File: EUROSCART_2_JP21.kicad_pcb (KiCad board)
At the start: 2 copper layers, 52.8 x 42.2 mm, 2 parts

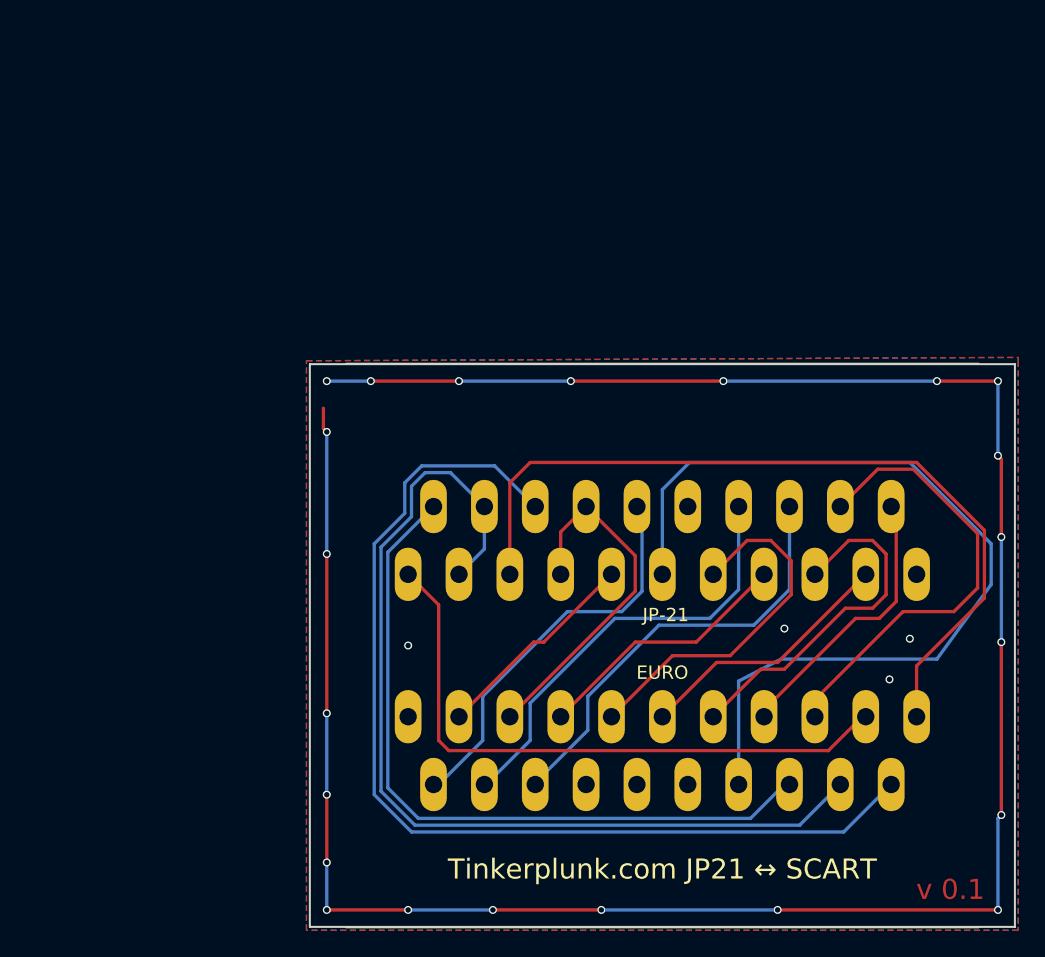
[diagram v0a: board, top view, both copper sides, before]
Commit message: revised to use one female and one male
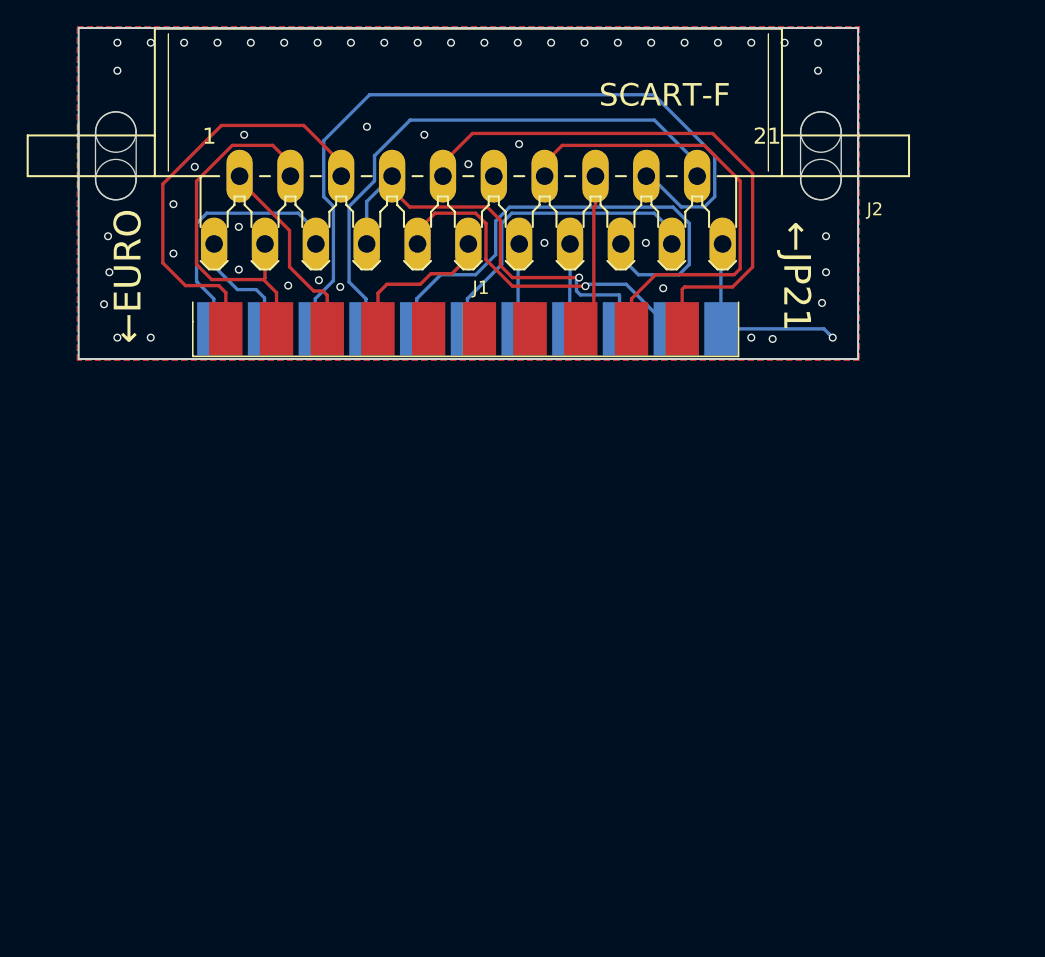
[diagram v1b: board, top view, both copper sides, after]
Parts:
- removed EURO, JP-21: SCART-F, SCART-RIGHT-ANGLE:SCART Right Angle
- added J1: SCART-F, Tinkerplunk:MALE_SCART, F.Cu at (113.2, 93.8)
- added J2: SCART-F, Tinkerplunk:SCART-F-RA, F.Cu at (133.8, 80.4)
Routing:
- net GND: track 178.1 -> 15.1 mm, vias 26 -> 51
- net 5V: track 67.3 -> 11.6 mm
- net RT_IN: track 77.2 -> 31.6 mm
- net A_GND: track 73.3 -> 29.2 mm
- net RT_OUT: track 61.2 -> 19.2 mm
- net L_IN: track 54.6 -> 14.6 mm
- net L_OUT: track 46.8 -> 8.74 mm
- net B_GND: track 34.4 -> 57.8 mm
- net BLU: track 21.1 -> 42.6 mm
- net BLANK: track 32.9 -> 11.9 mm
- net R_GND: track 27.3 -> 6.40 mm
- net RED: track 19.7 -> 6.40 mm
- net S_IN: track 30.1 -> 42.3 mm
- net G_GND: track 26.6 -> 37.6 mm
- net S_OUT: track 15.8 -> 26.7 mm, vias 0 -> 1
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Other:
- board size 52.8 x 42.2 mm -> 58.4 x 24.8 mm
- board text added: "EUROSCART⇄JP21 BIDIRECTIONAL"
- board text added: "←EURO"
- board text added: "←JP21"
- board text removed: "Tinkerplunk.com JP21 ↔ SCART"
- board text removed: "v 0.1"

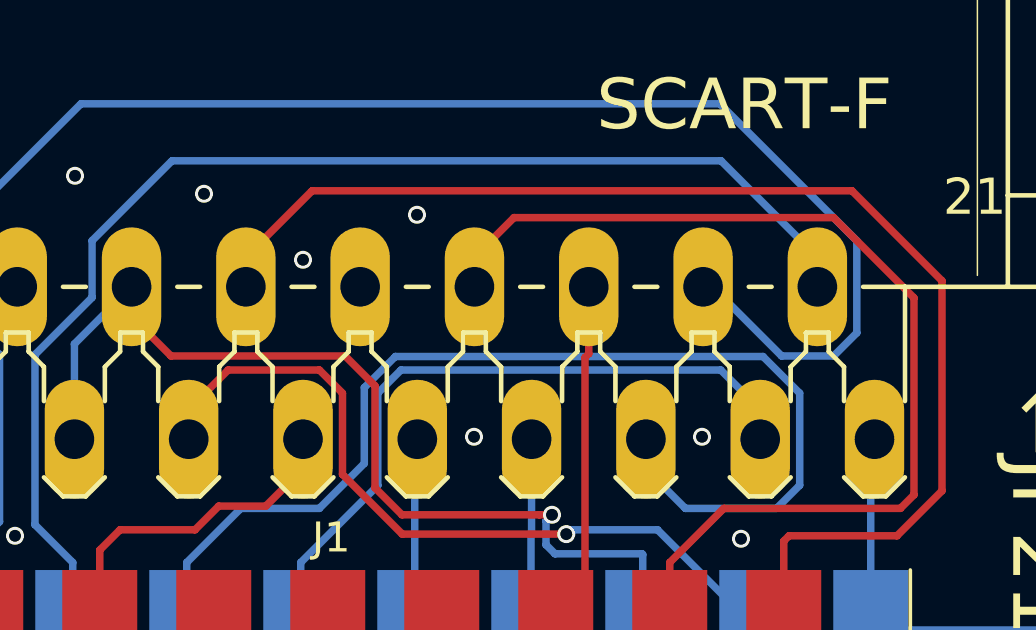
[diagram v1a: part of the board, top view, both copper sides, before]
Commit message: Fixed swapped sync pins on JP21
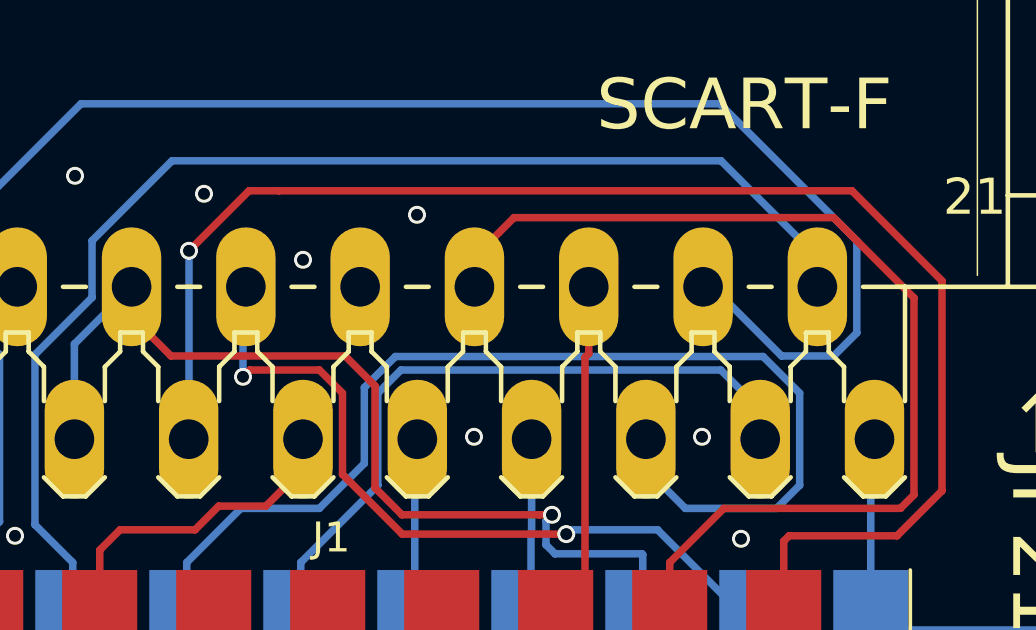
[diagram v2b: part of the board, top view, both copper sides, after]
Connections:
- J2 pad 10: S_IN -> S_OUT
- J2 pad 9: S_OUT -> S_IN
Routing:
- net S_IN: track 42.3 -> 49.4 mm, vias 0 -> 1
- net S_OUT: track 26.7 -> 26.4 mm, vias 1 -> 2
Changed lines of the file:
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@@
     (thickness 1.6)
     (drawings 9)
-    (tracks 208)
+    (tracks 213)
     (zones 0)
     (modules 2)
@@
     (mod_text_size 1 1)
     (mod_text_width 0.15)
-    (pad_size 1.524 1.524)
-    (pad_drill 0.762)
+    (pad_size 3.9624 1.9812)
+    (pad_drill 1.3208)
     (pad_to_mask_clearance 0.2)
     (aux_axis_origin 0 0)
@@
       (net 8 S_GND) (solder_mask_margin 0.1016))
     (pad 9 thru_hole oval (at 3.81 -5.08 270) (size 3.9624 1.9812) (drill 1.3208) (layers *.Cu *.Mask)
+      (net 11 S_IN) (solder_mask_margin 0.1016))
+    (pad 10 thru_hole oval (at 1.905 0 270) (size 3.9624 1.9812) (drill 1.3208) (layers *.Cu *.Mask)
       (net 10 S_OUT) (solder_mask_margin 0.1016))
-    (pad 10 thru_hole oval (at 1.905 0 270) (size 3.9624 1.9812) (drill 1.3208) (layers *.Cu *.Mask)
-      (net 11 S_IN) (solder_mask_margin 0.1016))
     (pad 11 thru_hole oval (at 0 -5.08 270) (size 3.9624 1.9812) (drill 1.3208) (layers *.Cu *.Mask)
       (net 20 5V) (solder_mask_margin 0.1016))
@@
   (gr_line (start 104.6 94.1) (end 163 94.1) (layer Edge.Cuts) (width 0.15))
   (gr_line (start 104.6 69.3) (end 104.6 94.1) (layer Edge.Cuts) (width 0.15))
-  (via (at 160 70.4) (size 0.6) (drill 0.4) (layers F.Cu B.Cu) (net 12))
-  (via (at 157.5 70.4) (size 0.6) (drill 0.4) (layers F.Cu B.Cu) (net 12))
-  (via (at 155 70.4) (size 0.6) (drill 0.4) (layers F.Cu B.Cu) (net 12))
-  (via (at 152.5 70.4) (size 0.6) (drill 0.4) (layers F.Cu B.Cu) (net 12))
-  (via (at 150 70.4) (size 0.6) (drill 0.4) (layers F.Cu B.Cu) (net 12))
-  (via (at 147.5 70.4) (size 0.6) (drill 0.4) (layers F.Cu B.Cu) (net 12))
-  (via (at 145 70.4) (size 0.6) (drill 0.4) (layers F.Cu B.Cu) (net 12))
-  (via (at 142.5 70.4) (size 0.6) (drill 0.4) (layers F.Cu B.Cu) (net 12))
-  (via (at 140 70.4) (size 0.6) (drill 0.4) (layers F.Cu B.Cu) (net 12))
-  (via (at 137.5 70.4) (size 0.6) (drill 0.4) (layers F.Cu B.Cu) (net 12))
-  (via (at 135 70.4) (size 0.6) (drill 0.4) (layers F.Cu B.Cu) (net 12))
-  (via (at 132.5 70.4) (size 0.6) (drill 0.4) (layers F.Cu B.Cu) (net 12))
-  (via (at 130 70.4) (size 0.6) (drill 0.4) (layers F.Cu B.Cu) (net 12))
-  (via (at 127.5 70.4) (size 0.6) (drill 0.4) (layers F.Cu B.Cu) (net 12))
-  (via (at 125 70.4) (size 0.6) (drill 0.4) (layers F.Cu B.Cu) (net 12))
-  (via (at 122.5 70.4) (size 0.6) (drill 0.4) (layers F.Cu B.Cu) (net 12))
-  (via (at 120 70.4) (size 0.6) (drill 0.4) (layers F.Cu B.Cu) (net 12))
-  (via (at 117.5 70.4) (size 0.6) (drill 0.4) (layers F.Cu B.Cu) (net 12))
-  (via (at 115 70.4) (size 0.6) (drill 0.4) (layers F.Cu B.Cu) (net 12))
-  (via (at 112.5 70.4) (size 0.6) (drill 0.4) (layers F.Cu B.Cu) (net 12))
-  (via (at 110 70.4) (size 0.6) (drill 0.4) (layers F.Cu B.Cu) (net 12))
-  (via (at 107.5 70.4) (size 0.6) (drill 0.4) (layers F.Cu B.Cu) (net 12))
   (segment (start 149.04 84.4894) (end 149.04 85.48) (width 0.25) (layer B.Cu) (net 4))
   (segment (start 147.72439 83.17379) (end 149.04 84.4894) (width 0.25) (layer B.Cu) (net 4))
@@
   (segment (start 142.55001 88.5) (end 142.55001 88.618731) (width 0.25) (layer B.Cu) (net 10))
   (segment (start 142.55001 88.618731) (end 142.575 88.643721) (width 0.25) (layer B.Cu) (net 10))
-  (segment (start 129.99 84.4894) (end 129.99 85.48) (width 0.25) (layer F.Cu) (net 10))
-  (segment (start 131.30561 83.17379) (end 129.99 84.4894) (width 0.25) (layer F.Cu) (net 10))
+  (segment (start 132.02621 83.17379) (end 131.8 83.4) (width 0.25) (layer F.Cu) (net 10))
+  (segment (start 134.344943 83.17379) (end 132.02621 83.17379) (width 0.25) (layer F.Cu) (net 10))
   (segment (start 135.11561 83.944457) (end 134.344943 83.17379) (width 0.25) (layer F.Cu) (net 10))
   (segment (start 135.11561 86.65202) (end 135.11561 83.944457) (width 0.25) (layer F.Cu) (net 10))
+  (segment (start 142.575 88.643721) (end 137.107311 88.643721) (width 0.25) (layer F.Cu) (net 10))
   (segment (start 137.107311 88.643721) (end 135.11561 86.65202) (width 0.25) (layer F.Cu) (net 10))
-  (segment (start 134.344943 83.17379) (end 131.30561 83.17379) (width 0.25) (layer F.Cu) (net 10))
-  (segment (start 142.575 88.643721) (end 137.107311 88.643721) (width 0.25) (layer F.Cu) (net 10))
-  (segment (start 150 88.7) (end 149.825 88.875) (width 0.25) (layer F.Cu) (net 11))
+  (via (at 131.8 83.4) (size 0.6) (drill 0.4) (layers F.Cu B.Cu) (net 10))
+  (segment (start 131.8 80.495) (end 131.895 80.4) (width 0.25) (layer B.Cu) (net 10))
+  (segment (start 131.8 83.4) (end 131.8 80.495) (width 0.25) (layer B.Cu) (net 10))
   (segment (start 149.825 88.875) (end 149.825 91.840501) (width 0.25) (layer F.Cu) (net 11))
-  (segment (start 153.6 88.7) (end 150 88.7) (width 0.25) (layer F.Cu) (net 11))
-  (segment (start 131.895 79.4094) (end 134.1044 77.2) (width 0.25) (layer F.Cu) (net 11))
-  (segment (start 131.895 80.4) (end 131.895 79.4094) (width 0.25) (layer F.Cu) (net 11))
-  (segment (start 134.1044 77.2) (end 152.1 77.2) (width 0.25) (layer F.Cu) (net 11))
   (segment (start 152.1 77.2) (end 155.1 80.2) (width 0.25) (layer F.Cu) (net 11))
+  (segment (start 133 77.2) (end 152.1 77.2) (width 0.25) (layer F.Cu) (net 11))
   (segment (start 155.1 80.2) (end 155.1 87.2) (width 0.25) (layer F.Cu) (net 11))
   (segment (start 155.1 87.2) (end 153.6 88.7) (width 0.25) (layer F.Cu) (net 11))
+  (segment (start 153.6 88.7) (end 150 88.7) (width 0.25) (layer F.Cu) (net 11))
+  (segment (start 150 88.7) (end 149.825 88.875) (width 0.25) (layer F.Cu) (net 11))
+  (via (at 130 79.2) (size 0.6) (drill 0.4) (layers F.Cu B.Cu) (net 11))
+  (segment (start 133 77.2) (end 132 77.2) (width 0.25) (layer F.Cu) (net 11))
+  (segment (start 132 77.2) (end 130 79.2) (width 0.25) (layer F.Cu) (net 11))
+  (segment (start 130 85.47) (end 129.99 85.48) (width 0.25) (layer B.Cu) (net 11))
+  (segment (start 130 79.2) (end 130 85.47) (width 0.25) (layer B.Cu) (net 11))
+  (via (at 160 70.4) (size 0.6) (drill 0.4) (layers F.Cu B.Cu) (net 12))
+  (via (at 157.5 70.4) (size 0.6) (drill 0.4) (layers F.Cu B.Cu) (net 12))
+  (via (at 155 70.4) (size 0.6) (drill 0.4) (layers F.Cu B.Cu) (net 12))
+  (via (at 152.5 70.4) (size 0.6) (drill 0.4) (layers F.Cu B.Cu) (net 12))
+  (via (at 150 70.4) (size 0.6) (drill 0.4) (layers F.Cu B.Cu) (net 12))
+  (via (at 147.5 70.4) (size 0.6) (drill 0.4) (layers F.Cu B.Cu) (net 12))
+  (via (at 145 70.4) (size 0.6) (drill 0.4) (layers F.Cu B.Cu) (net 12))
+  (via (at 142.5 70.4) (size 0.6) (drill 0.4) (layers F.Cu B.Cu) (net 12))
+  (via (at 140 70.4) (size 0.6) (drill 0.4) (layers F.Cu B.Cu) (net 12))
+  (via (at 137.5 70.4) (size 0.6) (drill 0.4) (layers F.Cu B.Cu) (net 12))
+  (via (at 135 70.4) (size 0.6) (drill 0.4) (layers F.Cu B.Cu) (net 12))
+  (via (at 132.5 70.4) (size 0.6) (drill 0.4) (layers F.Cu B.Cu) (net 12))
+  (via (at 130 70.4) (size 0.6) (drill 0.4) (layers F.Cu B.Cu) (net 12))
+  (via (at 127.5 70.4) (size 0.6) (drill 0.4) (layers F.Cu B.Cu) (net 12))
+  (via (at 125 70.4) (size 0.6) (drill 0.4) (layers F.Cu B.Cu) (net 12))
+  (via (at 122.5 70.4) (size 0.6) (drill 0.4) (layers F.Cu B.Cu) (net 12))
+  (via (at 120 70.4) (size 0.6) (drill 0.4) (layers F.Cu B.Cu) (net 12))
+  (via (at 117.5 70.4) (size 0.6) (drill 0.4) (layers F.Cu B.Cu) (net 12))
+  (via (at 115 70.4) (size 0.6) (drill 0.4) (layers F.Cu B.Cu) (net 12))
+  (via (at 112.5 70.4) (size 0.6) (drill 0.4) (layers F.Cu B.Cu) (net 12))
+  (via (at 110 70.4) (size 0.6) (drill 0.4) (layers F.Cu B.Cu) (net 12))
+  (via (at 107.5 70.4) (size 0.6) (drill 0.4) (layers F.Cu B.Cu) (net 12))
   (via (at 155 92.5) (size 0.6) (drill 0.4) (layers F.Cu B.Cu) (net 12))
   (via (at 160 72.5) (size 0.6) (drill 0.4) (layers F.Cu B.Cu) (net 12))
